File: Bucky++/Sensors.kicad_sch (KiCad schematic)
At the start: 25 parts, among them IC1 INA239AQDGSRQ1, IC2 INA239AQDGSRQ1, IC2001 INA239AQDGSRQ1, IC3 INA239AQDGSRQ1, IC6 INA239AQDGSRQ1

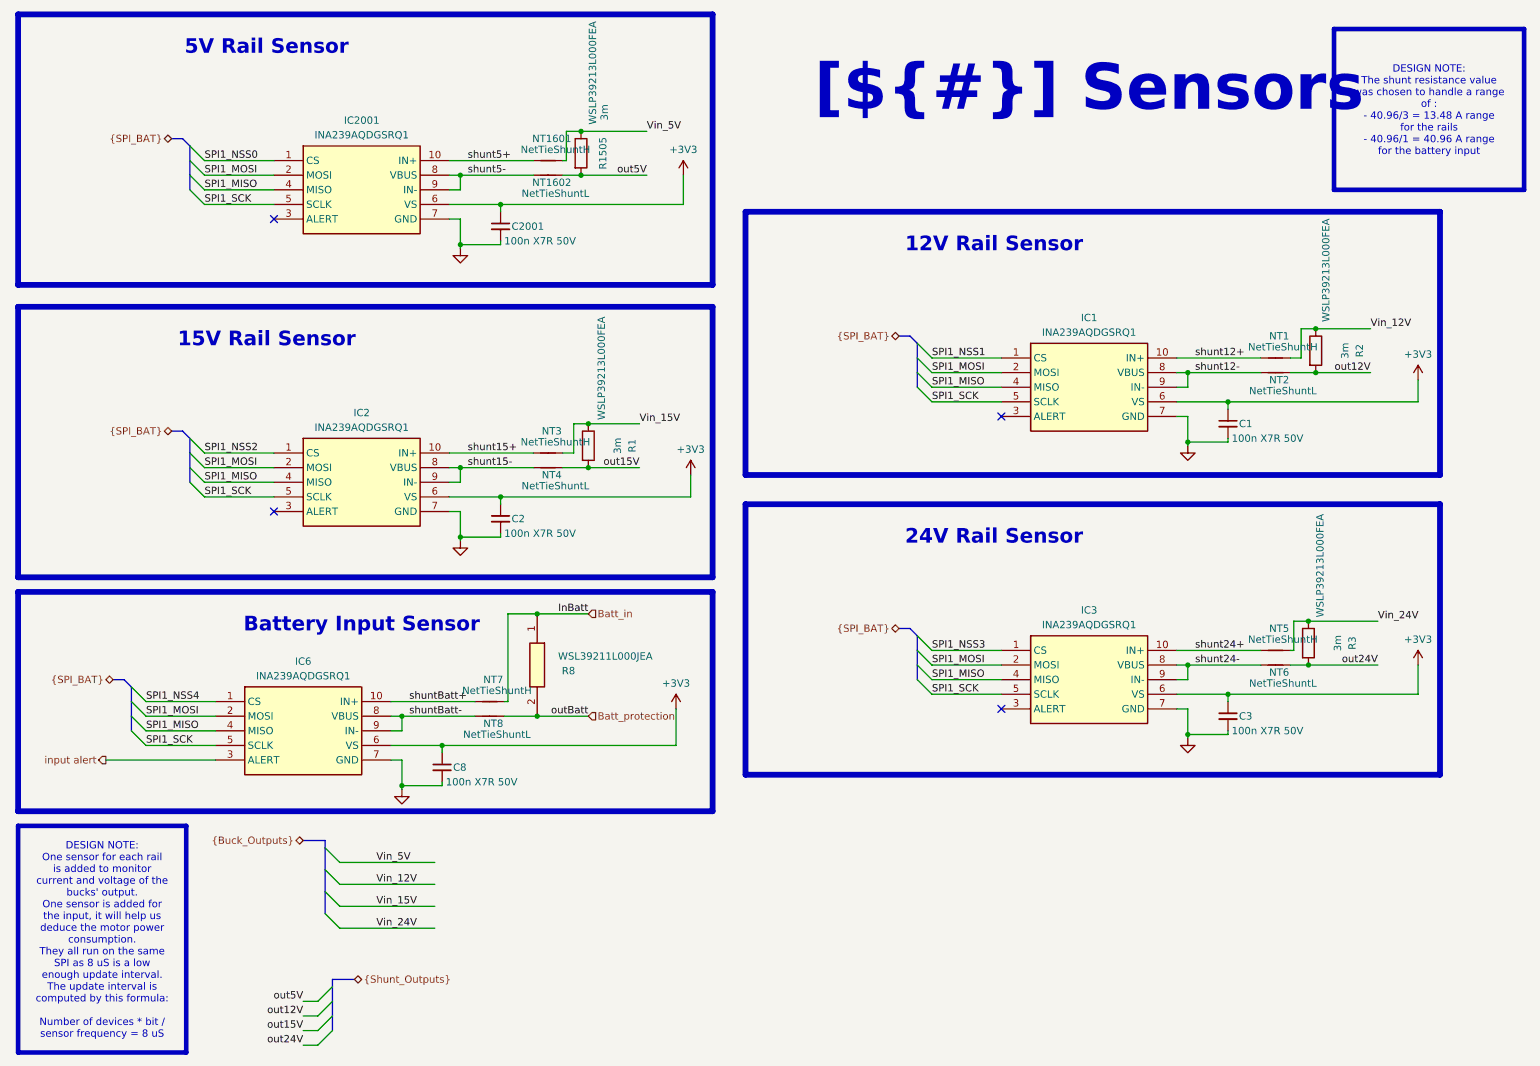
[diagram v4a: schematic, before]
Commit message: connected alert pins of each rail
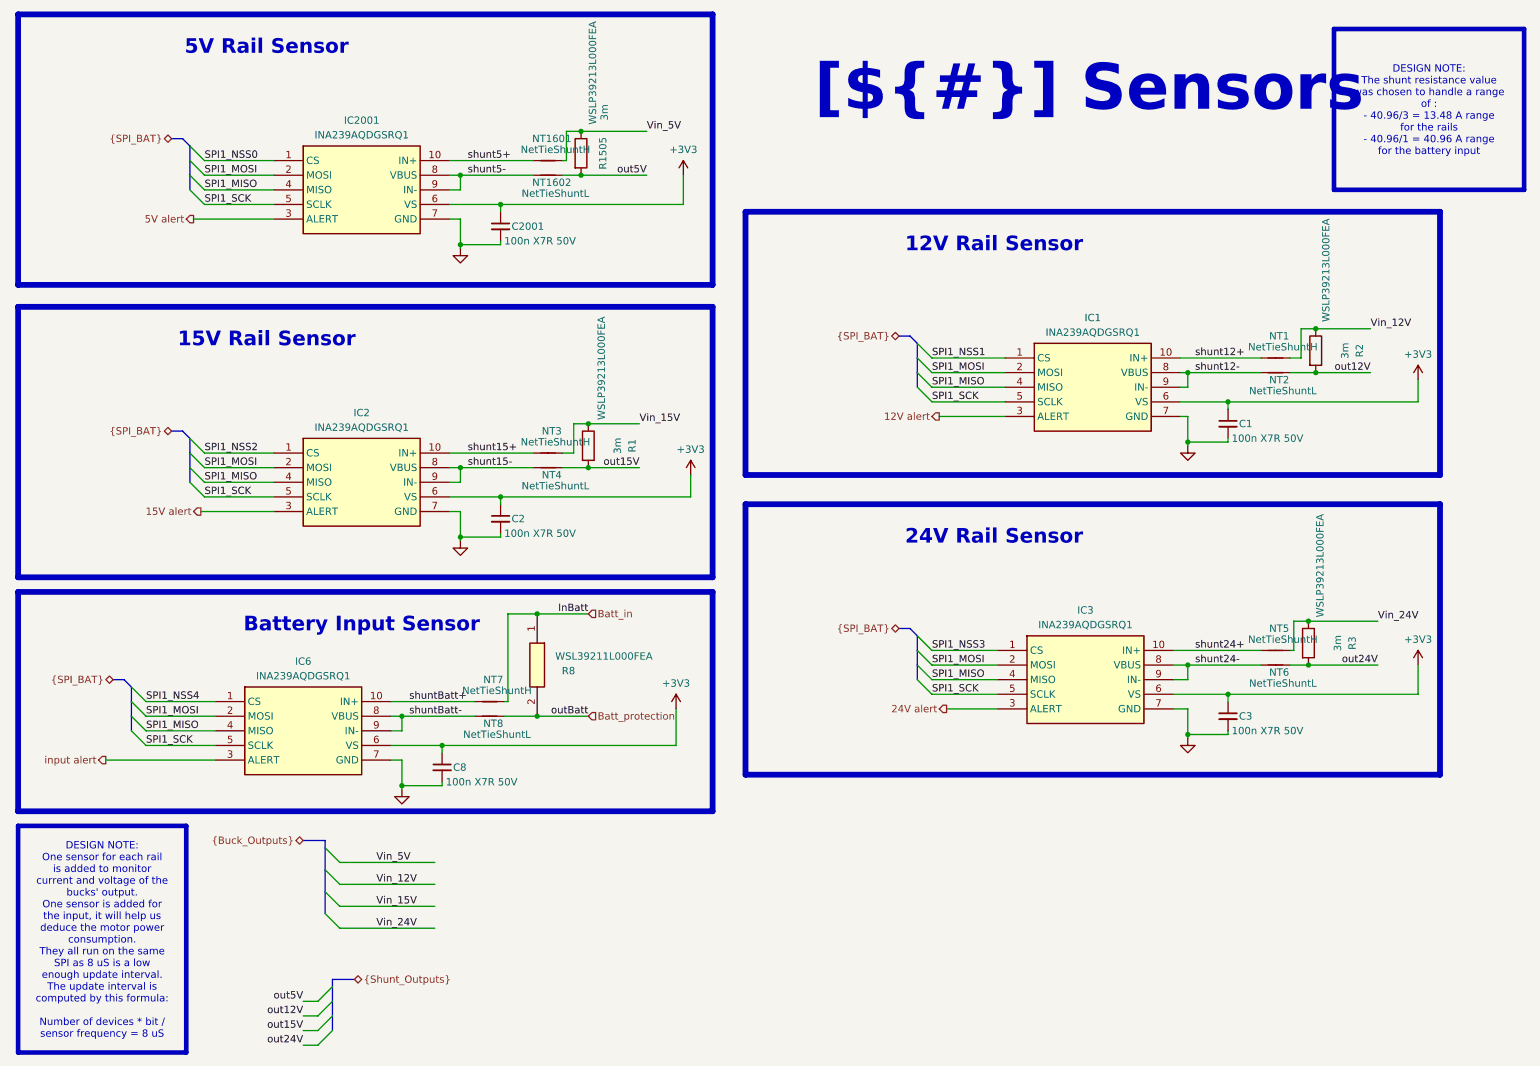
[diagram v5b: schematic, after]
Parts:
- R8: value WSL39211L000JEA -> WSL39211L000FEA
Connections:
- net 12V alert: now reaches IC1.3 (ALERT)
- net 5V alert: now reaches IC2001.3 (ALERT)
- net 24V alert: now reaches IC3.3 (ALERT)
- net 15V alert: now reaches IC2.3 (ALERT)
- no-connect marks 4 -> 0
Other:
- moved on the sheet: IC1, IC3
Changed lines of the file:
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@@
 		(color 0 0 0 0)
 	)
-	(no_connect
-		(at 187.325 85.09)
-	)
-	(no_connect
-		(at 187.325 135.89)
-	)
-	(no_connect
-		(at 60.96 50.8)
-	)
-	(no_connect
-		(at 60.96 101.6)
-	)
 	(bus_entry
 		(at 69.85 160.02)
@@
 	(wire
 		(pts
-			(xy 175.26 128.27) (xy 187.325 128.27)
+			(xy 175.26 128.27) (xy 186.69 128.27)
 		)
 		(stroke
@@
 	(wire
 		(pts
-			(xy 175.26 133.35) (xy 187.325 133.35)
+			(xy 175.26 133.35) (xy 186.69 133.35)
 		)
 		(stroke
@@
 	(wire
 		(pts
-			(xy 217.805 74.93) (xy 232.41 74.93)
+			(xy 218.44 74.93) (xy 232.41 74.93)
 		)
 		(stroke
@@
 	(wire
 		(pts
-			(xy 175.26 130.81) (xy 187.325 130.81)
+			(xy 175.26 130.81) (xy 186.69 130.81)
 		)
 		(stroke
@@
 	(wire
 		(pts
-			(xy 217.805 130.81) (xy 219.71 130.81)
+			(xy 217.17 130.81) (xy 219.71 130.81)
 		)
 		(stroke
@@
 	(wire
 		(pts
-			(xy 217.805 85.09) (xy 219.71 85.09)
+			(xy 218.44 85.09) (xy 219.71 85.09)
 		)
 		(stroke
@@
 	(wire
 		(pts
-			(xy 175.26 77.47) (xy 187.325 77.47)
+			(xy 175.26 77.47) (xy 187.96 77.47)
 		)
 		(stroke
@@
 	(wire
 		(pts
-			(xy 217.805 80.01) (xy 219.71 80.01)
+			(xy 218.44 80.01) (xy 219.71 80.01)
 		)
 		(stroke
@@
 	(wire
 		(pts
-			(xy 217.805 135.89) (xy 219.71 135.89)
+			(xy 217.17 135.89) (xy 219.71 135.89)
 		)
 		(stroke
@@
 	(wire
 		(pts
-			(xy 217.805 77.47) (xy 219.71 77.47)
+			(xy 218.44 77.47) (xy 219.71 77.47)
 		)
 		(stroke
@@
 	(wire
 		(pts
-			(xy 217.805 128.27) (xy 219.71 128.27)
+			(xy 217.17 128.27) (xy 219.71 128.27)
 		)
 		(stroke
@@
 	(wire
 		(pts
+			(xy 46.99 50.8) (xy 60.96 50.8)
+		)
+		(stroke
+			(width 0)
+			(type default)
+		)
+	)
+	(wire
+		(pts
 			(xy 113.03 86.36) (xy 115.57 86.36)
 		)
@@
 	(wire
 		(pts
-			(xy 217.805 133.35) (xy 226.695 133.35)
+			(xy 217.17 133.35) (xy 226.695 133.35)
+		)
+		(stroke
+			(width 0)
+			(type default)
+		)
+	)
+	(wire
+		(pts
+			(xy 48.26 101.6) (xy 60.96 101.6)
 		)
 		(stroke
@@
 	(wire
 		(pts
-			(xy 175.26 80.01) (xy 187.325 80.01)
+			(xy 175.26 80.01) (xy 187.96 80.01)
 		)
 		(stroke
@@
 	(wire
 		(pts
+			(xy 176.53 85.09) (xy 187.96 85.09)
+		)
+		(stroke
+			(width 0)
+			(type default)
+		)
+	)
+	(wire
+		(pts
 			(xy 83.185 149.225) (xy 83.185 149.86)
 		)
@@
 	(wire
 		(pts
-			(xy 175.26 74.93) (xy 187.325 74.93)
+			(xy 175.26 74.93) (xy 187.96 74.93)
 		)
 		(stroke
@@
 	(wire
 		(pts
-			(xy 217.805 82.55) (xy 226.695 82.55)
+			(xy 218.44 82.55) (xy 226.695 82.55)
 		)
 		(stroke
@@
 	(wire
 		(pts
-			(xy 217.805 125.73) (xy 232.41 125.73)
+			(xy 217.17 125.73) (xy 232.41 125.73)
 		)
 		(stroke
@@
 	(wire
 		(pts
-			(xy 175.26 82.55) (xy 187.325 82.55)
+			(xy 175.26 82.55) (xy 187.96 82.55)
 		)
 		(stroke
@@
 	(wire
 		(pts
+			(xy 177.8 135.89) (xy 186.69 135.89)
+		)
+		(stroke
+			(width 0)
+			(type default)
+		)
+	)
+	(wire
+		(pts
 			(xy 66.04 191.77) (xy 68.58 191.77)
 		)
@@
 	(wire
 		(pts
-			(xy 175.26 125.73) (xy 187.325 125.73)
+			(xy 175.26 125.73) (xy 186.69 125.73)
 		)
 		(stroke
@@
 		)
 	)
+	(hierarchical_label "24V alert"
+		(shape output)
+		(at 177.8 135.89 180)
+		(effects
+			(font
+				(size 1.27 1.27)
+			)
+			(justify right)
+		)
+	)
 	(hierarchical_label "{SPI_BAT}"
 		(shape bidirectional)
@@
 		)
 	)
+	(hierarchical_label "12V alert"
+		(shape output)
+		(at 176.53 85.09 180)
+		(effects
+			(font
+				(size 1.27 1.27)
+			)
+			(justify right)
+		)
+	)
 	(hierarchical_label "{SPI_BAT}"
 		(shape bidirectional)
@@
 		)
 	)
+	(hierarchical_label "5V alert"
+		(shape output)
+		(at 46.99 50.8 180)
+		(effects
+			(font
+				(size 1.27 1.27)
+			)
+			(justify right)
+		)
+	)
 	(hierarchical_label "{Shunt_Outputs}"
 		(shape tri_state)
@@
 		)
 	)
+	(hierarchical_label "15V alert"
+		(shape output)
+		(at 48.26 101.6 180)
+		(effects
+			(font
+				(size 1.27 1.27)
+			)
+			(justify right)
+		)
+	)
 	(symbol
 		(lib_id "power:+3V3")
@@
 	(symbol
 		(lib_id "INA239AQDGSRQ1:INA239AQDGSRQ1")
-		(at 187.325 74.93 0)
+		(at 187.96 74.93 0)
 		(unit 1)
 		(exclude_from_sim no)
@@
 		(fields_autoplaced yes)
 		(property "Reference" "IC1"
-			(at 202.565 67.945 0)
+			(at 203.2 67.945 0)
 			(effects
 				(font
@@
 		)
 		(property "Value" "INA239AQDGSRQ1"
-			(at 202.565 70.485 0)
+			(at 203.2 70.485 0)
 			(effects
 				(font
@@
 		)
 		(property "Footprint" "0_diode_smd:SOP50P490X110-10N"
-			(at 213.995 169.85 0)
+			(at 214.63 169.85 0)
 			(effects
 				(font
@@
 		)
 		(property "Datasheet" "https://www.ti.com/lit/ds/symlink/ina239-q1.pdf?ts=1649085907566&ref_url=https%253A%252F%252Fwww.ti.com%252Fproduct%252FINA239-Q1"
-			(at 213.995 269.85 0)
+			(at 214.63 269.85 0)
 			(effects
 				(font
@@
 		)
 		(property "Description" ""
-			(at 187.325 74.93 0)
+			(at 187.96 74.93 0)
 			(effects
 				(font
@@
 		)
 		(property "Height" "1.1"
-			(at 213.995 469.85 0)
+			(at 214.63 469.85 0)
 			(effects
 				(font
@@
 		)
 		(property "Mouser Part Number" "595-INA239AQDGSRQ1"
-			(at 213.995 569.85 0)
+			(at 214.63 569.85 0)
 			(effects
 				(font
@@
 		)
 		(property "Mouser Price/Stock" "https://www.mouser.co.uk/ProductDetail/Texas-Instruments/INA239AQDGSRQ1?qs=QNEnbhJQKva5RO79sS938A%3D%3D"
-			(at 213.995 669.85 0)
+			(at 214.63 669.85 0)
 			(effects
 				(font
@@
 		)
 		(property "Manufacturer_Name" "Texas Instruments"
-			(at 213.995 769.85 0)
+			(at 214.63 769.85 0)
 			(effects
 				(font
@@
 		)
 		(property "Manufacturer_Part_Number" "INA239AQDGSRQ1"
-			(at 213.995 869.85 0)
+			(at 214.63 869.85 0)
 			(effects
 				(font
@@
 	(symbol
 		(lib_id "INA239AQDGSRQ1:INA239AQDGSRQ1")
-		(at 187.325 125.73 0)
+		(at 186.69 125.73 0)
 		(unit 1)
 		(exclude_from_sim no)
@@
 		(fields_autoplaced yes)
 		(property "Reference" "IC3"
-			(at 202.565 118.745 0)
+			(at 201.93 118.745 0)
 			(effects
 				(font
@@
 		)
 		(property "Value" "INA239AQDGSRQ1"
-			(at 202.565 121.285 0)
+			(at 201.93 121.285 0)
 			(effects
 				(font
@@
 		)
 		(property "Footprint" "0_diode_smd:SOP50P490X110-10N"
-			(at 213.995 220.65 0)
+			(at 213.36 220.65 0)
 			(effects
 				(font
@@
 		)
 		(property "Datasheet" "https://www.ti.com/lit/ds/symlink/ina239-q1.pdf?ts=1649085907566&ref_url=https%253A%252F%252Fwww.ti.com%252Fproduct%252FINA239-Q1"
-			(at 213.995 320.65 0)
+			(at 213.36 320.65 0)
 			(effects
 				(font
@@
 		)
 		(property "Description" ""
-			(at 187.325 125.73 0)
+			(at 186.69 125.73 0)
 			(effects
 				(font
@@
 		)
 		(property "Height" "1.1"
-			(at 213.995 520.65 0)
+			(at 213.36 520.65 0)
 			(effects
 				(font
@@
 		)
 		(property "Mouser Part Number" "595-INA239AQDGSRQ1"
-			(at 213.995 620.65 0)
+			(at 213.36 620.65 0)
 			(effects
 				(font
@@
 		)
 		(property "Mouser Price/Stock" "https://www.mouser.co.uk/ProductDetail/Texas-Instruments/INA239AQDGSRQ1?qs=QNEnbhJQKva5RO79sS938A%3D%3D"
-			(at 213.995 720.65 0)
+			(at 213.36 720.65 0)
 			(effects
 				(font
@@
 		)
 		(property "Manufacturer_Name" "Texas Instruments"
-			(at 213.995 820.65 0)
+			(at 213.36 820.65 0)
 			(effects
 				(font
@@
 		)
 		(property "Manufacturer_Part_Number" "INA239AQDGSRQ1"
-			(at 213.995 920.65 0)
+			(at 213.36 920.65 0)
 			(effects
 				(font
@@
 			)
 		)
-		(property "Value" "WSL39211L000JEA"
+		(property "Value" "WSL39211L000FEA"
 			(at 126.746 126.746 90)
 			(effects
@@
 			)
 		)
-		(property "Description" "1 mOhms +/-5% 3W Chip Resistor Nonstandard Anti-Sulfur, Automotive AEC-Q200, Current Sense, Moisture Resistant, Pulse Withstanding Metal Element"
+		(property "Description" "1 mOhms +/-1% 3W Chip Resistor Nonstandard Anti-Sulfur, Automotive AEC-Q200, Current Sense, Moisture Resistant, Pulse Withstanding Metal Element"
 			(at 106.68 119.38 0)
 			(effects

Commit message: Cleared DRC errors, corrected routing errors, cleaned the schematic
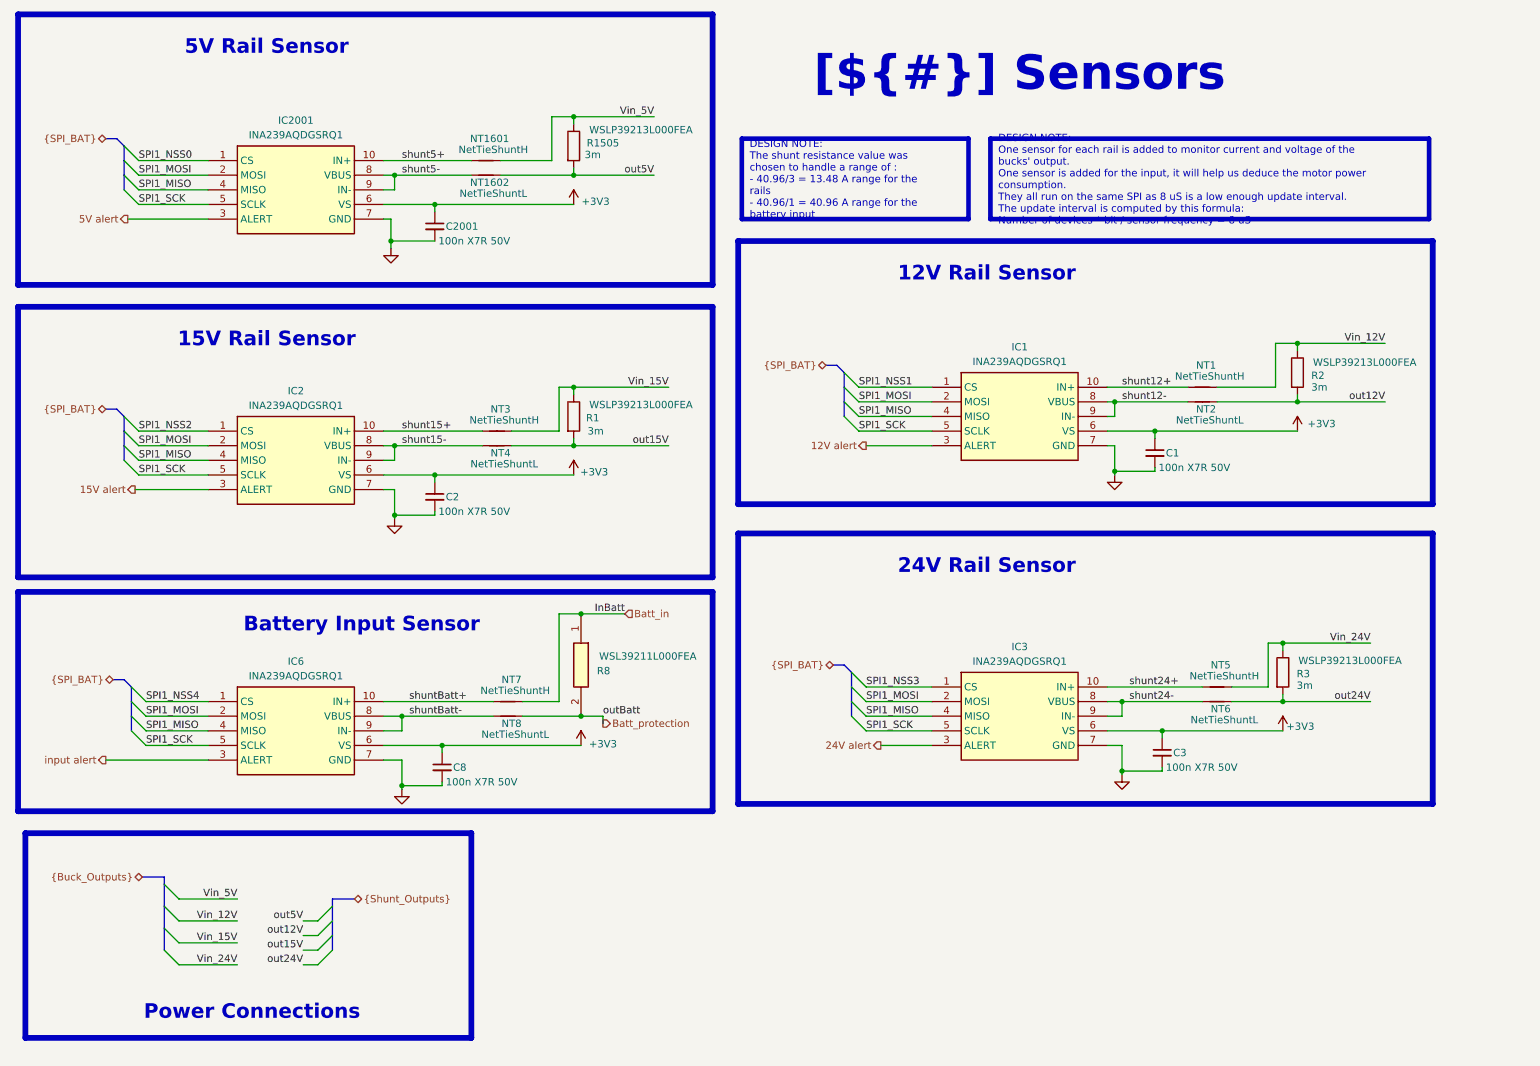
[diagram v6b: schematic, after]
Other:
- moved on the sheet: C1, C2, C2001, C3, IC1, IC2, IC2001, IC3, IC6, NT1, NT1601, NT1602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
